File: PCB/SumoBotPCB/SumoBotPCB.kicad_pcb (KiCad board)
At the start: 2 copper layers, 90 x 62.5 mm, 23 parts, among them M1 Motor_DC, M2 Motor_DC, M3 Motor_DC, M4 Motor_DC, SW1 SW_Push, U1 TB6612FNG, U10 VL53L0X-GY530, U11 VL53L0X-GY530, U12 VL53L0X-GY530, U2 hc-05_BLUETOOTH_MODULE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

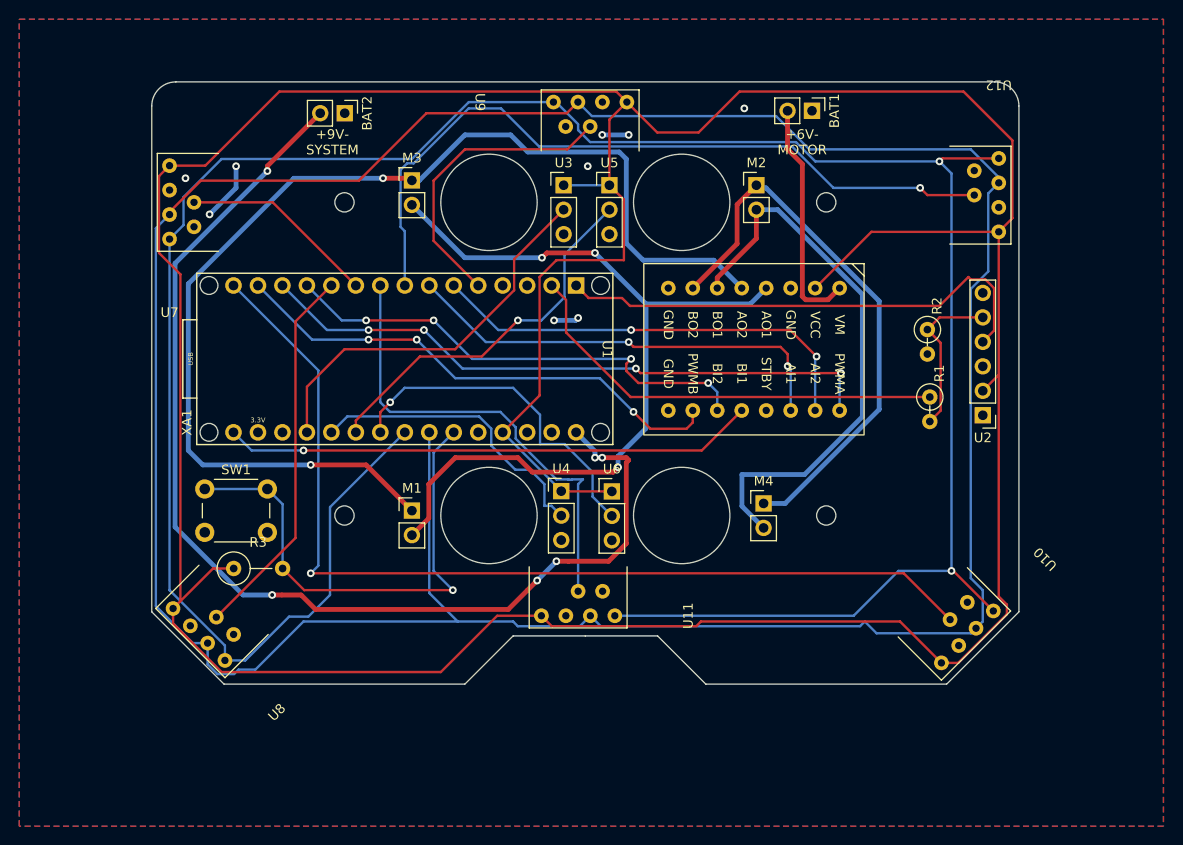
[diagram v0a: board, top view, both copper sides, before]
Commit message: motor driver pwm
correct pin assignment to have motor driver use 6 pwm pins to allow all options.
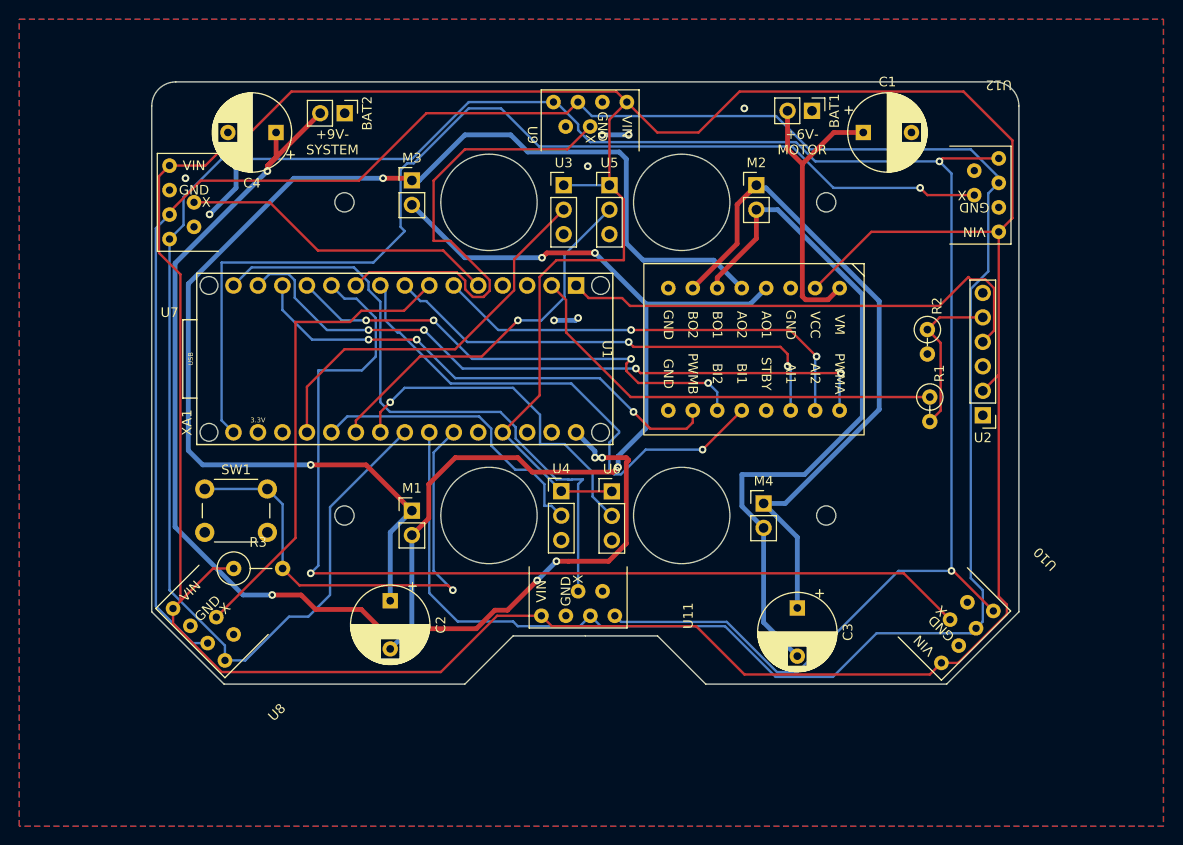
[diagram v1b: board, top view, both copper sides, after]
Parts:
- added C1: C_Polarized_US, Capacitor_THT:CP_Radial_D8.0mm_P5.00mm, F.Cu at (203.8, 50.2)
- added C2: C_Polarized_US, Capacitor_THT:CP_Radial_D8.0mm_P5.00mm, F.Cu at (154.8, 98.8)
- added C3: C_Polarized_US, Capacitor_THT:CP_Radial_D8.0mm_P5.00mm, F.Cu at (197.0, 99.6)
- added C4: C_Polarized_US, Capacitor_THT:CP_Radial_D8.0mm_P5.00mm, F.Cu at (142.9, 50.2)
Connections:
- U1 pad 10: Net-(XA1-PadD11) -> Net-(U1-Pad10)
- U1 pad 14: Net-(XA1-PadD4) -> Net-(U1-Pad14)
- U1 pad 16: Net-(XA1-PadD10) -> Net-(U1-Pad16)
- U7 pad 5: Net-(U7-Pad5) -> Net-(XA1-PadD2)
- U8 pad 5: Net-(U8-Pad5) -> Net-(XA1-PadD4)
- U9 pad 5: Net-(U9-Pad5) -> Net-(XA1-PadD7)
- XA1 pad D10: Net-(XA1-PadD10) -> Net-(U1-Pad10)
- XA1 pad D11: Net-(XA1-PadD11) -> Net-(U1-Pad16)
- XA1 pad D12: Net-(U10-Pad5) -> Net-(U11-Pad5)
- XA1 pad D13: Net-(U1-Pad12) -> Net-(U12-Pad5)
- XA1 pad D2: Net-(U9-Pad5) -> Net-(XA1-PadD2)
- XA1 pad D5: Net-(U12-Pad5) -> Net-(U1-Pad14)
- XA1 pad D6: Net-(U11-Pad5) -> Net-(U1-Pad12)
- XA1 pad D7: Net-(U7-Pad5) -> Net-(XA1-PadD7)
- XA1 pad D8: Net-(U8-Pad5) -> Net-(U10-Pad5)
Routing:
- net Net-(U1-Pad16): track 0.00 -> 70.3 mm, vias 0 -> 4
- net Net-(XA1-PadD10): track 65.7 -> 0.00 mm, vias 4 -> 0
- net Net-(XA1-PadD11): track 52.8 -> 0.00 mm, vias 3 -> 0
- net Net-(U1-Pad10): track 0.00 -> 51.8 mm, vias 0 -> 3
- net Net-(XA1-PadD7): track 0.00 -> 49.8 mm
- net Net-(U1-Pad14): track 0.00 -> 48.7 mm, vias 0 -> 2
- net Net-(U8-Pad5): track 39.4 -> 0.00 mm
- net Net-(XA1-PadD2): track 0.00 -> 33.1 mm
- net Net-(U12-Pad5): track 78.1 -> 110.9 mm
- net Net-(U9-Pad5): track 31.4 -> 0.00 mm
- net Net-(U10-Pad3): track 298.8 -> 271.3 mm
- net Net-(U7-Pad5): track 20.4 -> 0.00 mm
- net Net-(U11-Pad5): track 49.0 -> 65.3 mm
- net Net-(M2-Pad2): track 58.6 -> 73.4 mm
- net Net-(M1-Pad2): track 87.9 -> 100.7 mm
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
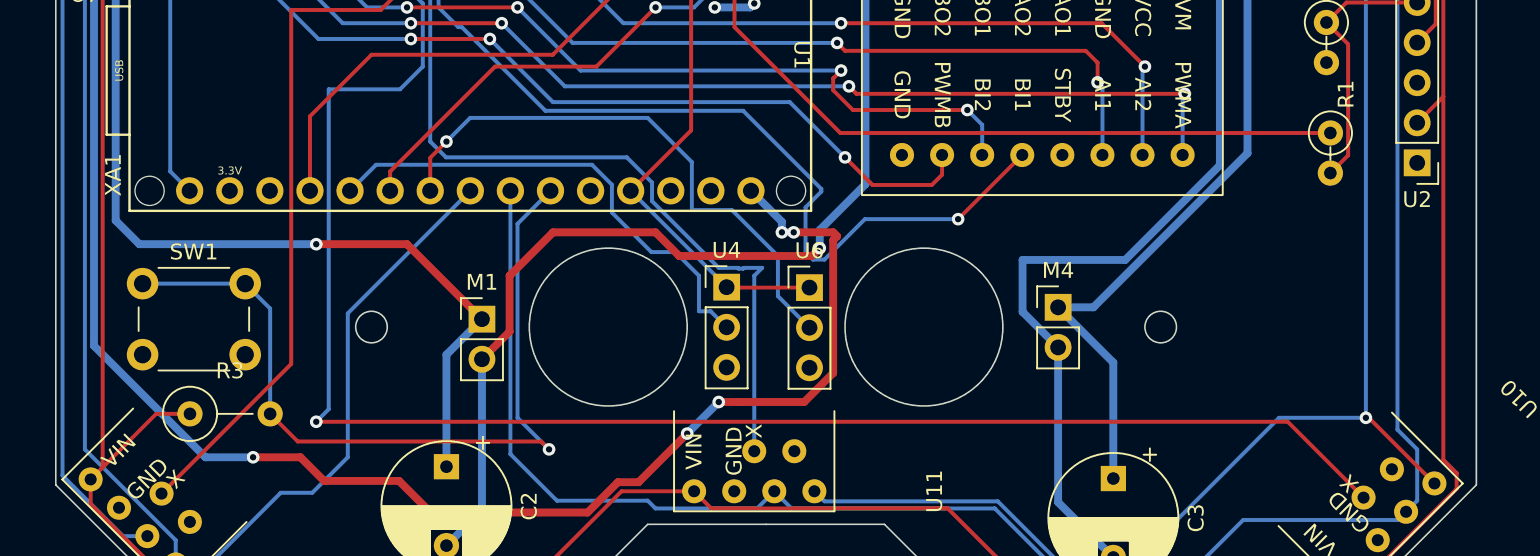
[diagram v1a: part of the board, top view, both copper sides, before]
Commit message: ADDED STANDBY SWITCH
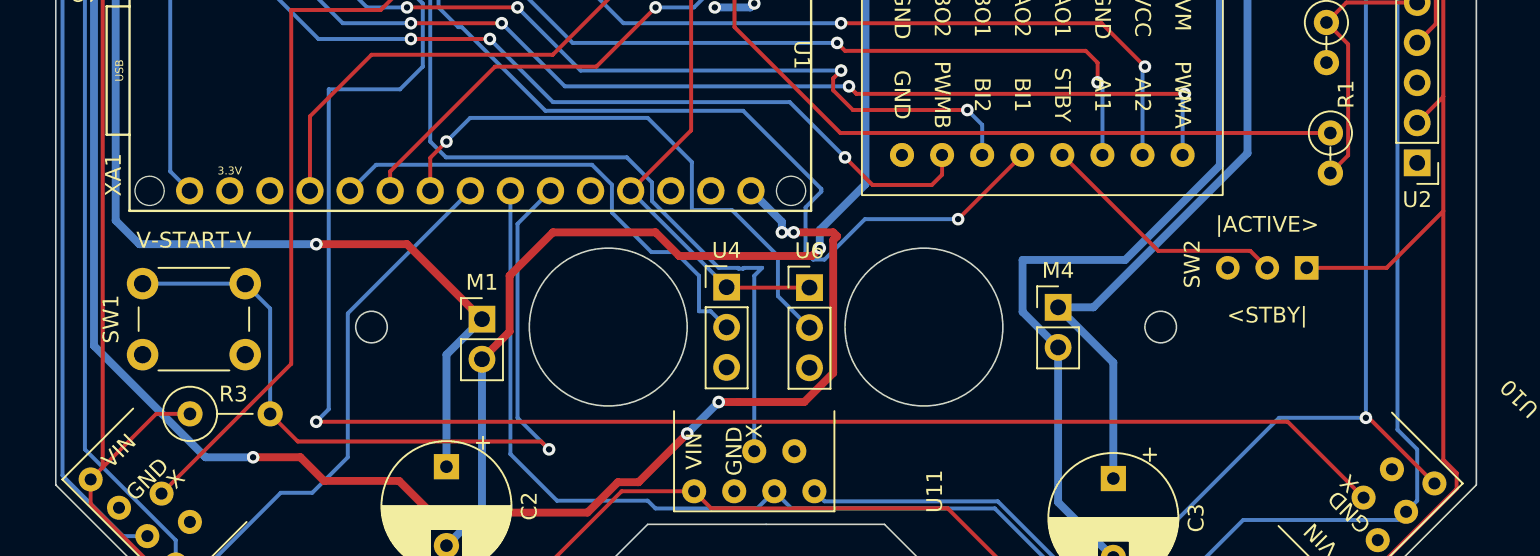
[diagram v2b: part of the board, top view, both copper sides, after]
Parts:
- added SW2: SW_SPDT, custom:SpDt SlideSwitch, F.Cu at (209.2, 86.2)
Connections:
- U1 pad 13: unconnected-(U1-Pad13) -> Net-(U1-Pad13)
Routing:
- net Net-(U1-Pad13): track 0.00 -> 15.9 mm
- net +5V: track 386.1 -> 396.2 mm
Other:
- board text added: "<STBY|"
- board text added: "V-START-V"
- board text added: "|ACTIVE>"
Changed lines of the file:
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@@
   (net 37 "Net-(U1-Pad16)")
   (net 38 "Net-(U1-Pad12)")
-  (net 39 "unconnected-(U1-Pad13)")
+  (net 39 "Net-(U1-Pad13)")
   (net 40 "Net-(XA1-PadD4)")
   (net 41 "Net-(XA1-PadD2)")
@@
   (net 43 "Net-(XA1-PadD7)")
   (net 44 "unconnected-(XA1-PadA7)")
+  (net 45 "unconnected-(SW2-Pad3)")
   (footprint "Connector_PinHeader_2.54mm:PinHeader_1x02_P2.54mm_Vertical" (layer "F.Cu")
     (at 157 55.225)
@@
     (property "Sheetname" "")
     (attr through_hole)
-    (fp_text reference "SW1" (at 3.25 -2) (layer "F.SilkS")
+    (fp_text reference "SW1" (at -2 2.25 -90) (layer "F.SilkS")
       (effects (font (size 1 1) (thickness 0.15)))
     )
@@
     (property "Sheetname" "")
     (attr through_hole)
-    (fp_text reference "R3" (at 2.54 -2.72) (layer "F.SilkS")
+    (fp_text reference "R3" (at 2.75 -1.25) (layer "F.SilkS")
       (effects (font (size 1 1) (thickness 0.15)))
     )
@@
     (pad "6" thru_hole circle (at 2.54 6.35) (size 1.524 1.524) (drill 0.762) (layers *.Cu *.Mask)
       (net 19 "unconnected-(U7-Pad6)") (pinfunction "G") (pintype "input"))
+  )
+  (footprint "custom:SpDt SlideSwitch" (layer "F.Cu")
+    (at 209.25 86.25 180)
+    (property "Sheetfile" "SumoBotPCB.kicad_sch")
+    (property "Sheetname" "")
+    (attr through_hole)
+    (fp_text reference "SW2" (at 7.25 0.25 90 unlocked) (layer "F.SilkS")
+      (effects (font (size 1 1) (thickness 0.15)))
+    )
+    (fp_text value "SW_SPDT" (at 0 1 180 unlocked) (layer "F.Fab")
+      (effects (font (size 1 1) (thickness 0.15)))
+    )
+    (fp_text user "${REFERENCE}" (at 0 2.5 180 unlocked) (layer "F.Fab")
+      (effects (font (size 1 1) (thickness 0.15)))
+    )
+    (fp_line (start -1.5 2) (end 6.5 2) (layer "F.CrtYd") (width 0.05))
+    (fp_line (start 6.5 2) (end 6.5 -2) (layer "F.CrtYd") (width 0.05))
+    (fp_line (start 6.5 -2) (end -1.5 -2) (layer "F.CrtYd") (width 0.05))
+    (fp_line (start -1.5 -2) (end -1.5 2) (layer "F.CrtYd") (width 0.05))
+    (pad "1" thru_hole rect (at 0 0 180) (size 1.5 1.5) (drill 0.8) (layers *.Cu *.Mask)
+      (net 9 "+5V") (pinfunction "A") (pintype "passive"))
+    (pad "2" thru_hole circle (at 2.5 0 180) (size 1.5 1.5) (drill 0.8) (layers *.Cu *.Mask)
+      (net 39 "Net-(U1-Pad13)") (pinfunction "B") (pintype "passive"))
+    (pad "3" thru_hole circle (at 5 0 180) (size 1.5 1.5) (drill 0.8) (layers *.Cu *.Mask)
+      (net 45 "unconnected-(SW2-Pad3)") (pinfunction "C") (pintype "passive"))
   )
   (footprint "custom:tb6612fng" (layer "F.Cu")
@@
       (net 38 "Net-(U1-Pad12)") (pinfunction "BI1") (pintype "input"))
     (pad "13" thru_hole circle (at 12.7 7.62 270) (size 1.524 1.524) (drill 0.762) (layers *.Cu *.Mask)
-      (net 39 "unconnected-(U1-Pad13)") (pinfunction "STBY") (pintype "input"))
+      (net 39 "Net-(U1-Pad13)") (pinfunction "STBY") (pintype "input"))
     (pad "14" thru_hole circle (at 12.7 5.08 270) (size 1.524 1.524) (drill 0.762) (layers *.Cu *.Mask)
       (net 32 "Net-(U1-Pad14)") (pinfunction "AI1") (pintype "input"))
@@
     (effects (font (size 1 1) (thickness 0.15)))
   )
+  (gr_text "|ACTIVE>" (at 206.75 83.5) (layer "F.SilkS")
+    (effects (font (size 1 1) (thickness 0.15)))
+  )
   (gr_text "+9V-\nSYSTEM" (at 148.75 51.25) (layer "F.SilkS")
+    (effects (font (size 1 1) (thickness 0.15)))
+  )
+  (gr_text "<STBY|" (at 206.75 89.25) (layer "F.SilkS")
+    (effects (font (size 1 1) (thickness 0.15)))
+  )
+  (gr_text "V-START-V" (at 138.75 84.5) (layer "F.SilkS")
     (effects (font (size 1 1) (thickness 0.15)))
   )
@@
   (segment (start 171.527 101.492) (end 186.508 101.492) (width 0.25) (layer "F.Cu") (net 9))
   (segment (start 135.56 53.69) (end 137.875 51.375) (width 0.25) (layer "F.Cu") (net 9))
+  (segment (start 217.905 82.655) (end 217.905 98.405) (width 0.25) (layer "F.Cu") (net 9))
   (segment (start 218.75 100.25) (end 213.703949 105.296051) (width 0.25) (layer "F.Cu") (net 9))
   (segment (start 139.125 51.375) (end 144.5 46) (width 0.25) (layer "F.Cu") (net 9))
@@
   (segment (start 179 57.225) (end 177.5 55.725) (width 0.25) (layer "F.Cu") (net 9))
   (segment (start 186.508 101.492) (end 191.516 106.5) (width 0.25) (layer "F.Cu") (net 9))
+  (segment (start 214.31 86.25) (end 209.25 86.25) (width 0.25) (layer "F.Cu") (net 9))
   (segment (start 198.85 66.4) (end 204.69 60.56) (width 0.25) (layer "F.Cu") (net 9))
   (segment (start 214.25 46) (end 219.32386 51.07386) (width 0.25) (layer "F.Cu") (net 9))
@@
   (segment (start 170.25 77.542) (end 170.25 65.25) (width 0.25) (layer "F.Cu") (net 9))
   (segment (start 136.361847 95.5) (end 138.5 95.5) (width 0.25) (layer "F.Cu") (net 9))
+  (segment (start 217.905 75.405) (end 217.905 82.655) (width 0.25) (layer "F.Cu") (net 9))
   (segment (start 191 46) (end 214.25 46) (width 0.25) (layer "F.Cu") (net 9))
   (segment (start 177.5 48.905) (end 179.31 47.095) (width 0.25) (layer "F.Cu") (net 9))
@@
   (segment (start 166.422 81.37) (end 170.25 77.542) (width 0.25) (layer "F.Cu") (net 9))
   (segment (start 217.905 98.405) (end 218.75 99.25) (width 0.25) (layer "F.Cu") (net 9))
-  (segment (start 217.905 75.405) (end 217.905 98.405) (width 0.25) (layer "F.Cu") (net 9))
   (segment (start 191.516 106.5) (end 210.75 106.5) (width 0.25) (layer "F.Cu") (net 9))
   (segment (start 137.875 51.375) (end 139.125 51.375) (width 0.25) (layer "F.Cu") (net 9))
@@
   (segment (start 144.5 46) (end 178.215 46) (width 0.25) (layer "F.Cu") (net 9))
   (segment (start 160 106.25) (end 137.25 106.25) (width 0.25) (layer "F.Cu") (net 9))
+  (segment (start 217.905 82.655) (end 214.31 86.25) (width 0.25) (layer "F.Cu") (net 9))
   (segment (start 217.905 60.56) (end 217.905 75.405) (width 0.25) (layer "F.Cu") (net 9))
   (segment (start 204.69 60.56) (end 217.905 60.56) (width 0.25) (layer "F.Cu") (net 9))
@@
   (segment (start 161.024695 76.3) (end 155.724695 71) (width 0.25) (layer "B.Cu") (net 38))
   (segment (start 178.501849 81.418152) (end 178.501849 81.251849) (width 0.25) (layer "B.Cu") (net 38))
+  (segment (start 206.75 86.25) (end 205.675 85.175) (width 0.25) (layer "F.Cu") (net 39))
+  (segment (start 199.845 85.175) (end 193.77 79.1) (width 0.25) (layer "F.Cu") (net 39))
+  (segment (start 205.675 85.175) (end 199.845 85.175) (width 0.25) (layer "F.Cu") (net 39))
   (segment (start 151.75 68.75) (end 156.182 68.75) (width 0.25) (layer "F.Cu") (net 40))
   (segment (start 144.9134 69.9134) (end 150.5866 69.9134) (width 0.25) (layer "F.Cu") (net 40))

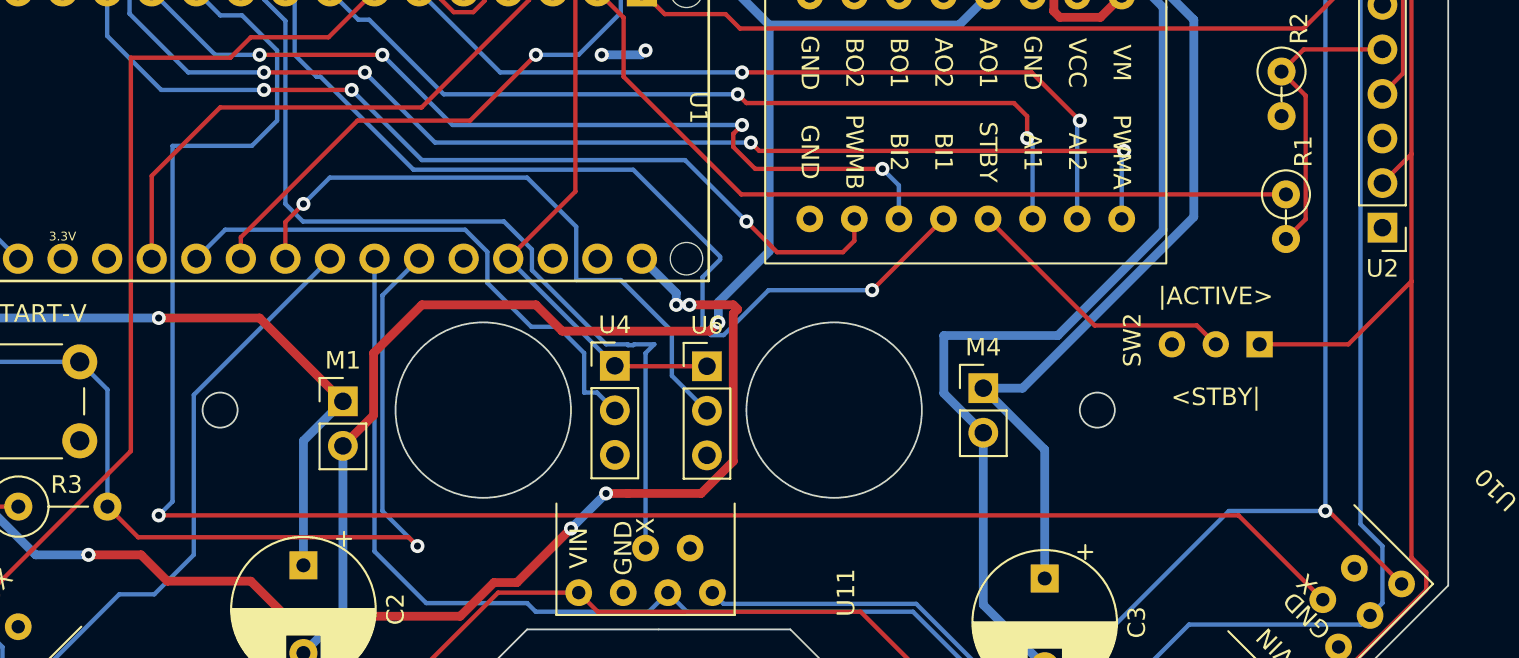
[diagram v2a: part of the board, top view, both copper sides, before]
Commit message: re-assigned pins
changed pin assignments on analog pins
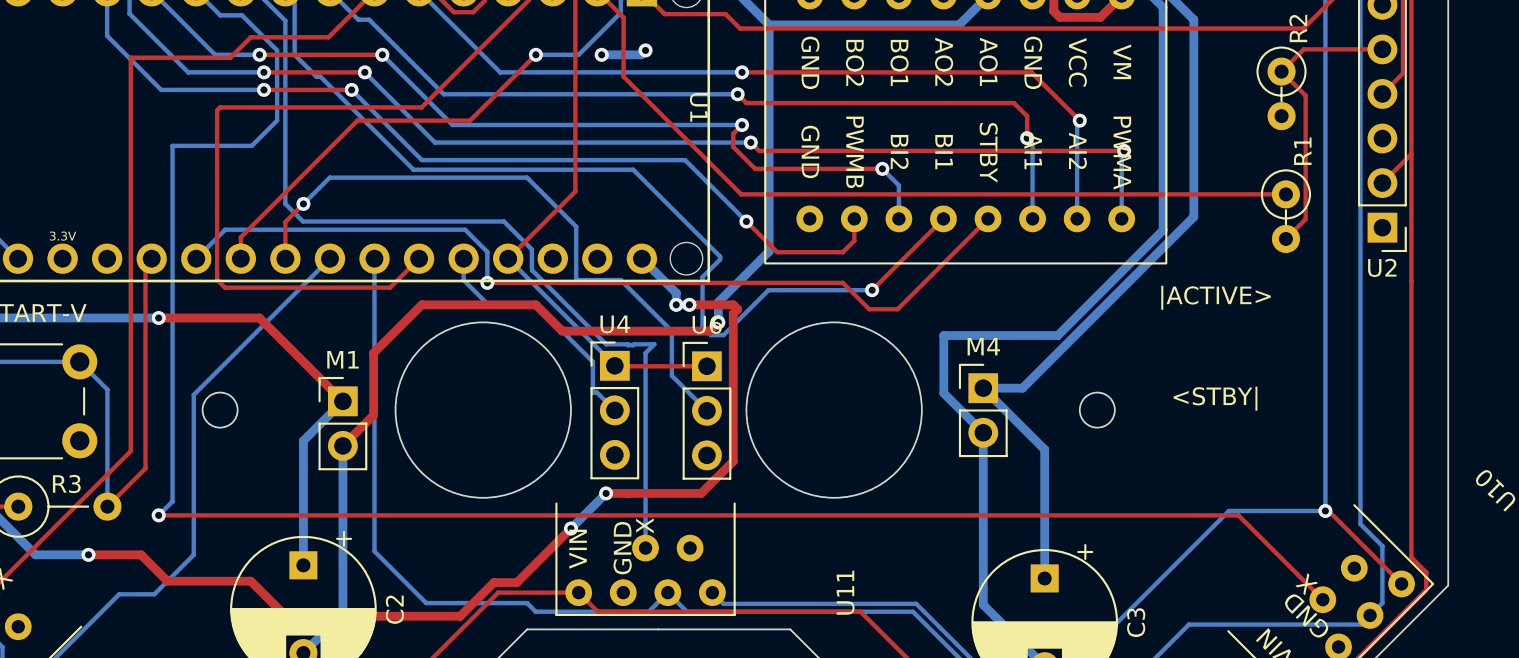
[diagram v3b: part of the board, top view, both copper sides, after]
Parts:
- removed SW2: SW_SPDT, custom:SpDt SlideSwitch
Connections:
- R3 pad 2: Net-(R3-Pad2) -> Net-(XA1-PadA0)
- SW1 pad 1: Net-(R3-Pad2) -> Net-(XA1-PadA0)
- U1 pad 13: Net-(U1-Pad13) -> Net-(XA1-PadA1)
- XA1 pad A0: Net-(U3-Pad2) -> Net-(XA1-PadA0)
- XA1 pad A1: Net-(U4-Pad2) -> Net-(XA1-PadA1)
- XA1 pad A6: Net-(R3-Pad2) -> Net-(U3-Pad2)
- XA1 pad A7: unconnected-(XA1-PadA7) -> Net-(U4-Pad2)
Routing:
- net Net-(R3-Pad2): track 52.1 -> 0.00 mm, vias 1 -> 0
- net Net-(XA1-PadA1): track 0.00 -> 50.9 mm, vias 0 -> 1
- net Net-(XA1-PadA0): track 0.00 -> 30.6 mm
- net Net-(U4-Pad2): track 31.2 -> 13.9 mm
- net Net-(U1-Pad13): track 15.9 -> 0.00 mm
- net Net-(U3-Pad2): track 40.9 -> 52.9 mm
- net +5V: track 396.2 -> 386.1 mm
